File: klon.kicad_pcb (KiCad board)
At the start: 2 copper layers, 69 parts, among them SW1 SW_DPDT_x2, U1 TL072, U2 LTC1044, U3 TL072

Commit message: update footprints, values
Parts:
- removed C1, C4: 0.1u, Capacitor_THT:C_Rect_L7.0mm_W4.5mm_P5.00mm
- removed C10: 82n, Capacitor_THT:C_Rect_L7.0mm_W4.5mm_P5.00mm
- removed C11, C14, C17, C2, C3, C7, C9: 1u, Capacitor_THT:CP_Radial_D4.0mm_P2.00mm
- removed C12, C22: 4.7u, Capacitor_THT:CP_Radial_D6.3mm_P2.50mm
- removed C13: 390p, Capacitor_THT:C_Rect_L7.0mm_W4.5mm_P5.00mm
- removed C15, C16: 47u, Capacitor_THT:CP_Radial_D6.3mm_P2.50mm
- removed C18: 2.2n, Capacitor_THT:C_Rect_L7.0mm_W4.5mm_P5.00mm
- removed C19: 27n, Capacitor_THT:C_Rect_L7.0mm_W4.5mm_P5.00mm
- removed C20: 820p, Capacitor_THT:C_Rect_L7.0mm_W4.5mm_P5.00mm
- removed C21: 3.9n, Capacitor_THT:C_Rect_L7.0mm_W4.5mm_P5.00mm
- removed C5, C8: 68n, Capacitor_THT:C_Rect_L7.0mm_W4.5mm_P5.00mm
- removed C6: 390n, Capacitor_THT:C_Rect_L7.0mm_W4.5mm_P5.00mm
- removed D1, D2: 1N4001, Diode_THT:D_5W_P10.16mm_Horizontal
- removed D3, D4: 1N34A, Diode_THT:D_5W_P10.16mm_Horizontal
- removed D5: 1N4742, Diode_THT:D_5W_P10.16mm_Horizontal
- removed D6: LED, Diode_THT:D_5W_P5.08mm_Vertical_KathodeUp
- removed GAIN_1, GAIN_2: 100K, Connector_PinHeader_1.27mm:PinHeader_2x03_P1.27mm_Vertical
- removed IN1, OUT1, PWR1: AudioJack2, klon:PinHeader_1x02_P1.27mm_Vertical_jack
- removed R1, R6: 10K, Resistor_THT:R_Axial_DIN0207_L6.3mm_D2.5mm_P10.16mm_Horizontal
- removed R10, R9: 15K, Resistor_THT:R_Axial_DIN0207_L6.3mm_D2.5mm_P10.16mm_Horizontal
- removed R11, R23, R25, R29: 100K, Resistor_THT:R_Axial_DIN0207_L6.3mm_D2.5mm_P10.16mm_Horizontal
- removed R12: 422K, Resistor_THT:R_Axial_DIN0207_L6.3mm_D2.5mm_P10.16mm_Horizontal
- removed R13, R26: 560, Resistor_THT:R_Axial_DIN0207_L6.3mm_D2.5mm_P10.16mm_Horizontal
- removed R14, R15, R19: 27K, Resistor_THT:R_Axial_DIN0207_L6.3mm_D2.5mm_P10.16mm_Horizontal
- removed R16, R5: 1K, Resistor_THT:R_Axial_DIN0207_L6.3mm_D2.5mm_P10.16mm_Horizontal
- removed R17: 22K, Resistor_THT:R_Axial_DIN0207_L6.3mm_D2.5mm_P10.16mm_Horizontal
- removed R18: 47K, Resistor_THT:R_Axial_DIN0207_L6.3mm_D2.5mm_P10.16mm_Horizontal
- removed R2: 1M, Resistor_THT:R_Axial_DIN0207_L6.3mm_D2.5mm_P10.16mm_Horizontal
- removed R20: 12K, Resistor_THT:R_Axial_DIN0207_L6.3mm_D2.5mm_P10.16mm_Horizontal
- removed R21: 392K, Resistor_THT:R_Axial_DIN0207_L6.3mm_D2.5mm_P10.16mm_Horizontal
- removed R22: 1K8, Resistor_THT:R_Axial_DIN0207_L6.3mm_D2.5mm_P10.16mm_Horizontal
- removed R24: 4K7, Resistor_THT:R_Axial_DIN0207_L6.3mm_D2.5mm_P10.16mm_Horizontal
- removed R27, R28: 68K, Resistor_THT:R_Axial_DIN0207_L6.3mm_D2.5mm_P10.16mm_Horizontal
- removed R3: 5K1, Resistor_THT:R_Axial_DIN0207_L6.3mm_D2.5mm_P10.16mm_Horizontal
- removed R30: 3K9, Resistor_THT:R_Axial_DIN0207_L6.3mm_D2.5mm_P10.16mm_Horizontal
- removed R4, R8: 1K5, Resistor_THT:R_Axial_DIN0207_L6.3mm_D2.5mm_P10.16mm_Horizontal
- removed R7: 2K, Resistor_THT:R_Axial_DIN0207_L6.3mm_D2.5mm_P10.16mm_Horizontal
- removed SW1: SW_DPDT_x2, Connector_PinHeader_1.27mm:PinHeader_2x03_P1.27mm_Vertical
- removed TONE1, VOL1: 10K, Connector_PinHeader_1.27mm:PinHeader_1x03_P1.27mm_Vertical
- removed U1, U3: TL072, Package_DIP:DIP-8_W7.62mm
- removed U2: LTC1044, Package_DIP:DIP-8_W7.62mm

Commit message: update footprints, add bypass LED circuit
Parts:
- added C1: 0.1u, Capacitor_THT:C_Rect_L7.0mm_W2.0mm_P5.00mm, F.Cu at (185.3, 58.0)
- added C10: 1u, Capacitor_THT:CP_Radial_D5.0mm_P2.50mm, F.Cu at (167.8, 105.9)
- added C11: 0.082u, Capacitor_THT:C_Rect_L7.0mm_W2.0mm_P5.00mm, F.Cu at (185.8, 78.9)
- added C12: 390p, Capacitor_THT:C_Rect_L7.0mm_W4.5mm_P5.00mm, F.Cu at (175.8, 88.6)
- added C13: 1u, Capacitor_THT:C_Rect_L7.0mm_W4.5mm_P5.00mm, F.Cu at (168.9, 96.5)
- added C14: 47u, Capacitor_THT:CP_Radial_D8.0mm_P3.80mm, F.Cu at (177.4, 77.2)
- added C15: 47u, Capacitor_THT:CP_Radial_D8.0mm_P3.80mm, F.Cu at (167.4, 82.7)
- added C16: 1u, Capacitor_THT:C_Rect_L7.0mm_W4.5mm_P5.00mm, F.Cu at (184.4, 85.0)
- added C17: 2200p, Capacitor_THT:C_Rect_L7.0mm_W2.0mm_P5.00mm, F.Cu at (158.9, 104.4)
- added C18: 0.027u, Capacitor_THT:C_Rect_L7.0mm_W2.0mm_P5.00mm, F.Cu at (141.0, 115.8)
- added C19: 820p, Capacitor_THT:C_Rect_L7.0mm_W4.5mm_P5.00mm, F.Cu at (149.5, 111.5)
- added C2: 1u, Capacitor_THT:CP_Radial_D5.0mm_P2.50mm, F.Cu at (159.3, 109.5)
- added C20: 4.7u, Capacitor_THT:C_Rect_L7.0mm_W6.5mm_P5.00mm, F.Cu at (160.4, 98.6)
- added C21: 3900p, Capacitor_THT:C_Rect_L7.0mm_W4.5mm_P5.00mm, F.Cu at (190.4, 62.8)
- added C22: 4.7u, Capacitor_THT:C_Rect_L7.0mm_W6.5mm_P5.00mm, F.Cu at (150.4, 104.5)
- added C3: 1u, Capacitor_THT:CP_Radial_D5.0mm_P2.50mm, F.Cu at (184.7, 91.3)
- added C4: 0.1u, Capacitor_THT:C_Rect_L7.0mm_W2.0mm_P5.00mm, F.Cu at (132.4, 115.8)
- added C5: 0.068u, Capacitor_THT:C_Rect_L7.0mm_W2.0mm_P5.00mm, F.Cu at (175.8, 83.8)
- added C6: 0.39u, Capacitor_THT:C_Rect_L7.0mm_W4.5mm_P5.00mm, F.Cu at (190.4, 68.9)
- added C7: 1u, Capacitor_THT:CP_Radial_D5.0mm_P2.50mm, F.Cu at (177.8, 94.9)
- added C8: 0.068u, Capacitor_THT:C_Rect_L7.0mm_W3.5mm_P5.00mm, F.Cu at (185.8, 74.6)
- added C9: 1u, Capacitor_THT:C_Rect_L7.0mm_W4.5mm_P5.00mm, F.Cu at (163.6, 90.5)
- added D1: 1N4001, Diode_THT:D_5W_P10.16mm_Horizontal, F.Cu at (138.8, 64.0)
- added D2: 1N4001, Diode_THT:D_5W_P10.16mm_Horizontal, F.Cu at (91.7, 106.6)
- added D3_ON1: LED, Diode_THT:D_5W_P5.08mm_Vertical_KathodeUp, F.Cu at (150.8, 97.7)
- added D4_OFF1: LED, Diode_THT:D_5W_P5.08mm_Vertical_KathodeUp, F.Cu at (166.5, 75.2)
- added D5: 1N4742, Diode_THT:D_5W_P10.16mm_Horizontal, F.Cu at (91.7, 111.8)
- added D5_CLIP1: 1N34A, Diode_THT:D_DO-15_P15.24mm_Horizontal, F.Cu at (126.4, 58.8)
- added D6_CLIP1: 1N34A, Diode_THT:D_DO-15_P15.24mm_Horizontal, F.Cu at (91.5, 101.4)
- added GAIN_1: 100K, Connector_PinHeader_1.27mm:PinHeader_2x03_P1.27mm_Vertical, F.Cu at (194.7, 73.6)
- added IN1: AudioJack2, Connector_Audio:Jack_6.35mm_Neutrik_NMJ4HFD2_Horizontal, F.Cu at (97.5, 58.8)
- added OUT1: AudioJack2, Connector_Audio:Jack_6.35mm_Neutrik_NMJ4HFD2_Horizontal, F.Cu at (97.5, 80.1)
- added PWR1: AudioJack2, Connector_BarrelJack:BarrelJack_Wuerth_6941xx301002, F.Cu at (129.9, 63.3)
- added R1: 10K, Resistor_THT:R_Axial_DIN0207_L6.3mm_D2.5mm_P10.16mm_Horizontal, F.Cu at (126.0, 92.1)
- added R10: 15K, Resistor_THT:R_Axial_DIN0207_L6.3mm_D2.5mm_P10.16mm_Horizontal, F.Cu at (123.6, 104.9)
- added R11: 422K, Resistor_THT:R_Axial_DIN0207_L6.3mm_D2.5mm_P10.16mm_Horizontal, F.Cu at (164.8, 70.4)
- added R12: 2K2, Resistor_THT:R_Axial_DIN0207_L6.3mm_D2.5mm_P10.16mm_Horizontal, F.Cu at (118.9, 108.9)
- added R13: 2K2, Resistor_THT:R_Axial_DIN0207_L6.3mm_D2.5mm_P10.16mm_Horizontal, F.Cu at (118.9, 113.0)
- added R14: 27K, Resistor_THT:R_Axial_DIN0207_L6.3mm_D2.5mm_P10.16mm_Horizontal, F.Cu at (166.0, 62.3)
- added R15: 27K, Resistor_THT:R_Axial_DIN0207_L6.3mm_D2.5mm_P10.16mm_Horizontal, F.Cu at (139.3, 80.8)
- added R16: 22K, Resistor_THT:R_Axial_DIN0207_L6.3mm_D2.5mm_P10.16mm_Horizontal, F.Cu at (139.3, 76.8)
- added R17: 1K, Resistor_THT:R_Axial_DIN0207_L6.3mm_D2.5mm_P10.16mm_Horizontal, F.Cu at (126.0, 96.2)
- added R18: 22K, Resistor_THT:R_Axial_DIN0207_L6.3mm_D2.5mm_P10.16mm_Horizontal, F.Cu at (139.3, 84.9)
- added R19: 47K, Resistor_THT:R_Axial_DIN0207_L6.3mm_D2.5mm_P10.16mm_Horizontal, F.Cu at (151.5, 72.7)
- added R2: 1M, Resistor_THT:R_Axial_DIN0207_L6.3mm_D2.5mm_P10.16mm_Horizontal, F.Cu at (105.6, 113.0)
- added R20: 27K, Resistor_THT:R_Axial_DIN0207_L6.3mm_D2.5mm_P10.16mm_Horizontal, F.Cu at (110.3, 100.8)
- added R21: 12K, Resistor_THT:R_Axial_DIN0207_L6.3mm_D2.5mm_P10.16mm_Horizontal, F.Cu at (164.8, 66.4)
- added R22: 392K, Resistor_THT:R_Axial_DIN0207_L6.3mm_D2.5mm_P10.16mm_Horizontal, F.Cu at (123.6, 100.8)
- added R23: 1K8, Resistor_THT:R_Axial_DIN0207_L6.3mm_D2.5mm_P10.16mm_Horizontal, F.Cu at (158.5, 58.3)
- added R24: 100K, Resistor_THT:R_Axial_DIN0207_L6.3mm_D2.5mm_P10.16mm_Horizontal, F.Cu at (105.6, 108.9)
- added R25: 100K, Resistor_THT:R_Axial_DIN0207_L6.3mm_D2.5mm_P10.16mm_Horizontal, F.Cu at (126.0, 88.1)
- added R26: 560, Resistor_THT:R_Axial_DIN0207_L6.3mm_D2.5mm_P10.16mm_Horizontal, F.Cu at (110.3, 104.9)
- added R27: 4K7, Resistor_THT:R_Axial_DIN0207_L6.3mm_D2.5mm_P10.16mm_Horizontal, F.Cu at (138.2, 72.7)
- added R28: 100K, Resistor_THT:R_Axial_DIN0207_L6.3mm_D2.5mm_P10.16mm_Horizontal, F.Cu at (126.0, 84.0)
- added R29: 560, Resistor_THT:R_Axial_DIN0207_L6.3mm_D2.5mm_P10.16mm_Horizontal, F.Cu at (152.7, 62.3)
- added R3: 5K1, Resistor_THT:R_Axial_DIN0207_L6.3mm_D2.5mm_P10.16mm_Horizontal, F.Cu at (126.0, 80.0)
- added R30: 68K, Resistor_THT:R_Axial_DIN0207_L6.3mm_D2.5mm_P10.16mm_Horizontal, F.Cu at (139.3, 93.0)
- added R31: 68K, Resistor_THT:R_Axial_DIN0207_L6.3mm_D2.5mm_P10.16mm_Horizontal, F.Cu at (138.2, 68.7)
- added R32: 100K, Resistor_THT:R_Axial_DIN0207_L6.3mm_D2.5mm_P10.16mm_Horizontal, F.Cu at (145.2, 58.3)
- added R4: 1K5, Resistor_THT:R_Axial_DIN0207_L6.3mm_D2.5mm_P10.16mm_Horizontal, F.Cu at (152.6, 80.8)
- added R5: 1K, Resistor_THT:R_Axial_DIN0207_L6.3mm_D2.5mm_P10.16mm_Horizontal, F.Cu at (136.9, 100.2)
- added R6: 1K5, Resistor_THT:R_Axial_DIN0207_L6.3mm_D2.5mm_P10.16mm_Horizontal, F.Cu at (152.6, 76.8)
- added R7: 10K, Resistor_THT:R_Axial_DIN0207_L6.3mm_D2.5mm_P10.16mm_Horizontal, F.Cu at (171.8, 58.3)
- added R8: 15K, Resistor_THT:R_Axial_DIN0207_L6.3mm_D2.5mm_P10.16mm_Horizontal, F.Cu at (151.5, 68.7)
- added R9: 2K, Resistor_THT:R_Axial_DIN0207_L6.3mm_D2.5mm_P10.16mm_Horizontal, F.Cu at (139.3, 88.9)
- added SW1: SW_DPDT_x2, Connector_PinHeader_1.27mm:PinHeader_2x03_P1.27mm_Vertical, F.Cu at (193.3, 82.3)
- added TONE1: 10K, Connector_PinHeader_1.27mm:PinHeader_1x03_P1.27mm_Vertical, F.Cu at (165.9, 110.9)
- added U1: TL072, Package_DIP:DIP-8_W7.62mm, F.Cu at (179.4, 62.4)
- added U2: LTC1044, Package_DIP:DIP-8_W7.62mm, F.Cu at (136.9, 104.3)
- added U3: TL072, Package_DIP:DIP-8_W7.62mm, F.Cu at (152.6, 84.9)
- added VOL1: 10K, Connector_PinHeader_1.27mm:PinHeader_1x03_P1.27mm_Vertical, F.Cu at (132.7, 108.6)

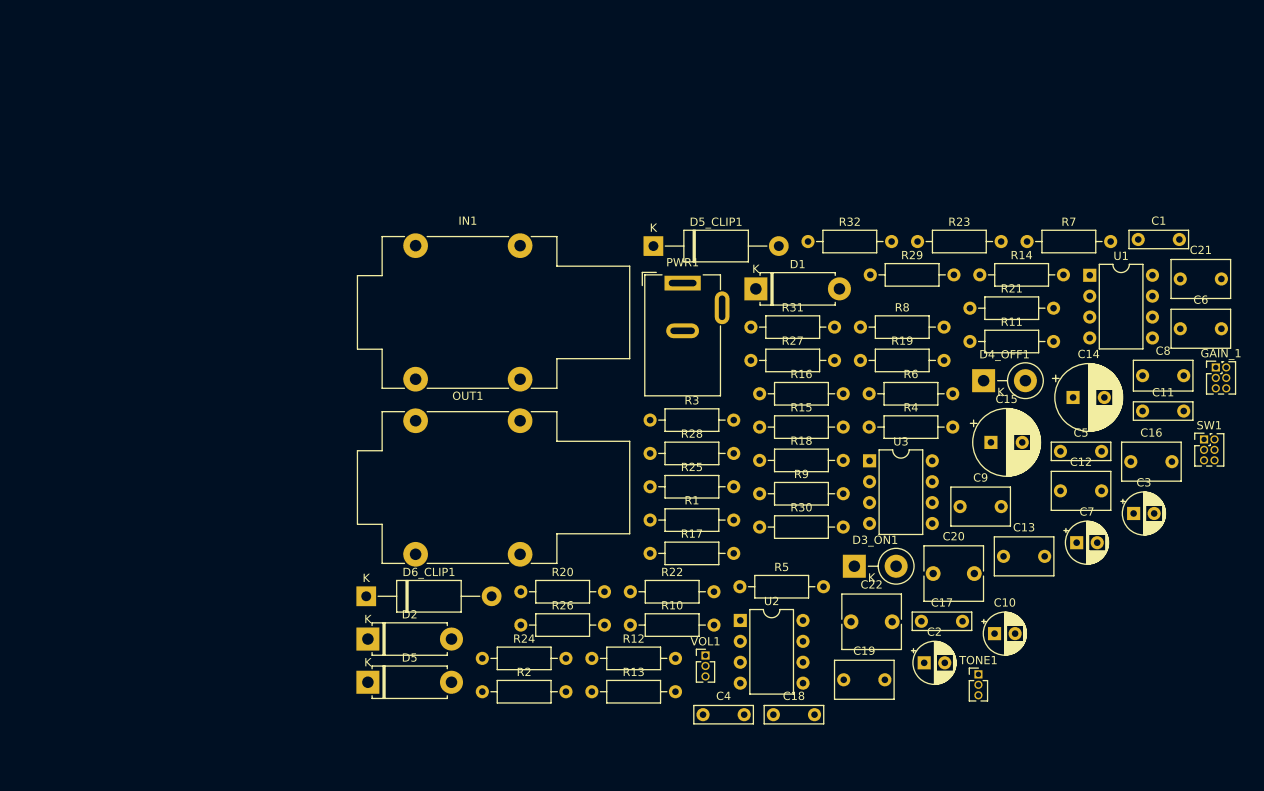
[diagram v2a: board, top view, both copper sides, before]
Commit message: add PCB layout
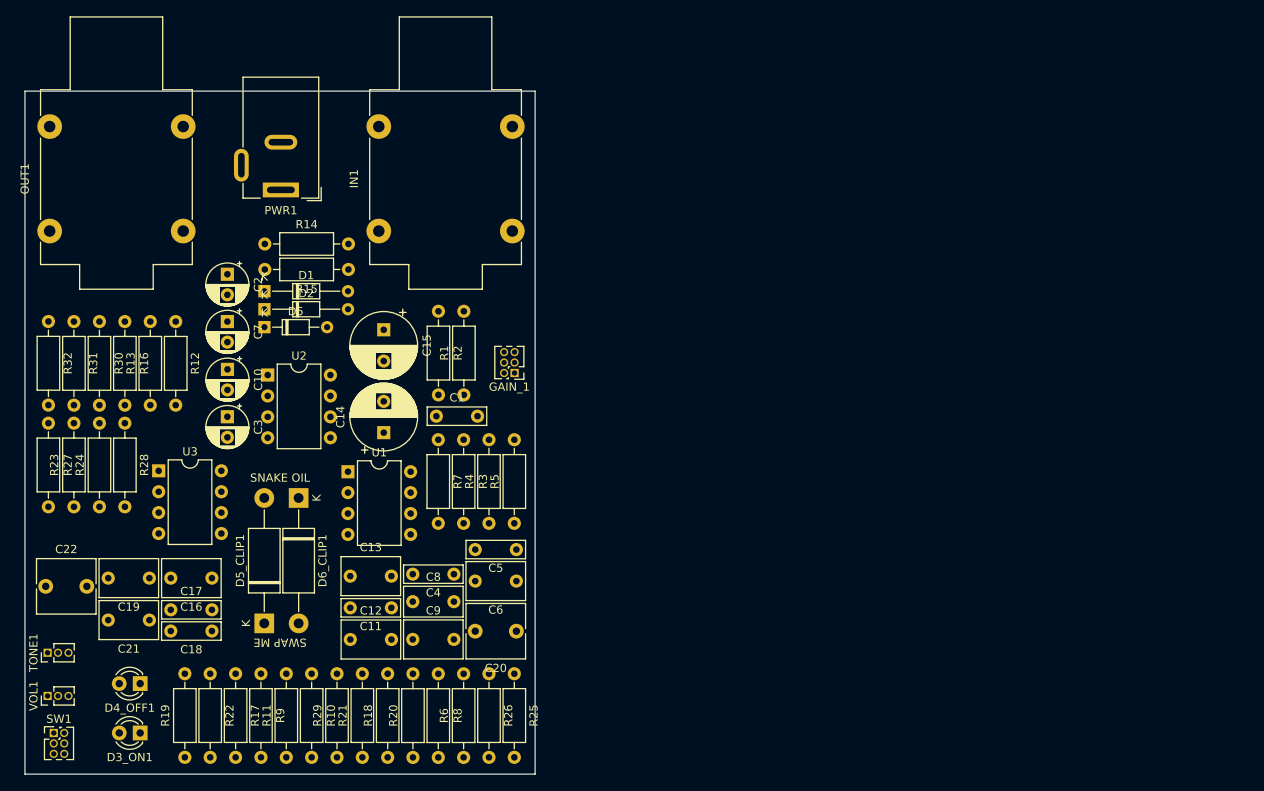
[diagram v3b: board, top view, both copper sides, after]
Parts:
- D1, D2: footprint Diode_THT:D_5W_P10.16mm_Horizontal -> Diode_THT:D_DO-34_SOD68_P10.16mm_Horizontal
- D3_ON1, D4_OFF1: footprint Diode_THT:D_5W_P5.08mm_Vertical_KathodeUp -> LED_THT:LED_D3.0mm_Clear
- D5: footprint Diode_THT:D_5W_P10.16mm_Horizontal -> Diode_THT:D_DO-34_SOD68_P7.62mm_Horizontal
- PWR1: value AudioJack2 -> Barrel_Jack
- moved SW1 144.3 mm to (53.5, 118.0)
- moved C21 132.0 mm to (65.1, 104.3), turned to 180 degrees
- moved TONE1 113.2 mm to (52.8, 108.2), turned to 90 degrees
- moved C16 112.6 mm to (72.7, 99.2), turned to 180 degrees
- moved C3 110.8 mm to (74.6, 79.6), turned to 270 degrees
- moved D4_OFF1 108.9 mm to (64.0, 112.0), turned to 180 degrees
- moved R23 107.5 mm to (56.0, 90.5), turned to 90 degrees
- moved C7 106.7 mm to (74.6, 68.0), turned to 270 degrees
- moved C10 98.6 mm to (74.6, 73.8), turned to 270 degrees
- moved C22 98.0 mm to (52.5, 100.2)
- moved R11 97.2 mm to (81.8, 121.0), turned to 90 degrees
- moved C2 97.0 mm to (74.6, 62.2), turned to 270 degrees
- moved R19 95.2 mm to (69.4, 121.0), turned to 90 degrees
- moved C11 94.4 mm to (94.5, 102.8), turned to 180 degrees
- moved U1 93.3 mm to (89.2, 86.2)
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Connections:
- PWR1 pad 1: (no net) -> +9V
- PWR1 pad 2: (no net) -> GND
- R2 pad 2: GND -> /+4.5V
- U1 pad 1: Net-(C20-Pad1) -> Net-(C12-Pad1)
- U1 pad 2: Net-(C20-Pad1) -> Net-(C8-Pad1)
- U1 pad 3: Net-(C1-Pad1) -> Net-(C11-Pad1)
- U1 pad 5: Net-(C8-Pad1) -> Net-(C20-Pad1)
- U1 pad 6: Net-(C11-Pad1) -> Net-(C1-Pad1)
- U1 pad 7: Net-(C12-Pad1) -> Net-(C20-Pad1)
- U3 pad 1: Net-(C19-Pad1) -> Net-(C22-Pad2)
- U3 pad 2: Net-(C18-Pad1) -> Net-(C21-Pad1)
- U3 pad 6: Net-(C21-Pad1) -> Net-(C18-Pad1)
- U3 pad 7: Net-(C22-Pad2) -> Net-(C19-Pad1)
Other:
- board outline added: 62 x 83 mm
- board text added: "SNAKE OIL"
- board text added: "SWAP ME"
